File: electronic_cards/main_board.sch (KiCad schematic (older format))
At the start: 9 parts, among them J1 Input1, J2 Input2, J3 Esp8266, J4 Vin, J5 IN 5V, J6 Output1, J7 Output2

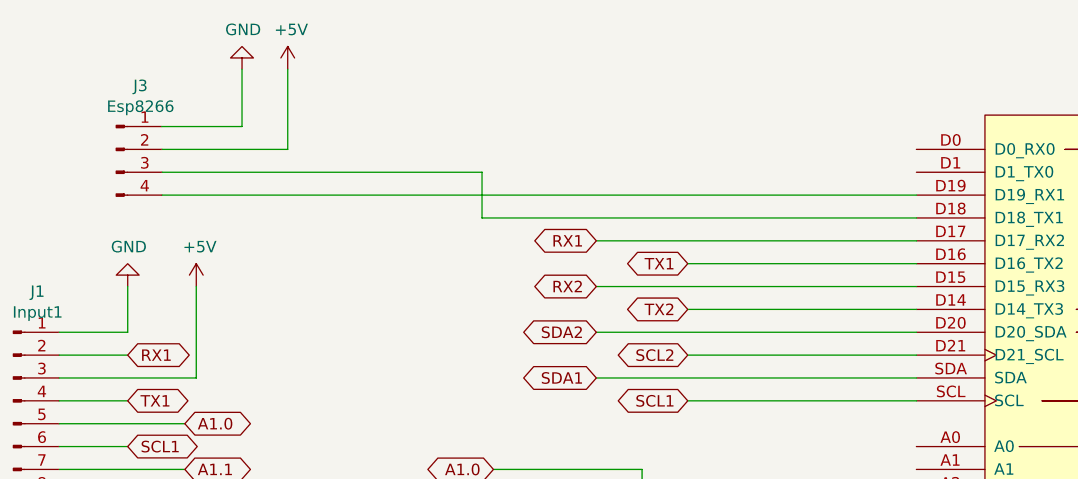
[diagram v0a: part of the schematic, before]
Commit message: Correctrion of PCB, RX and TX of ESP were inverted
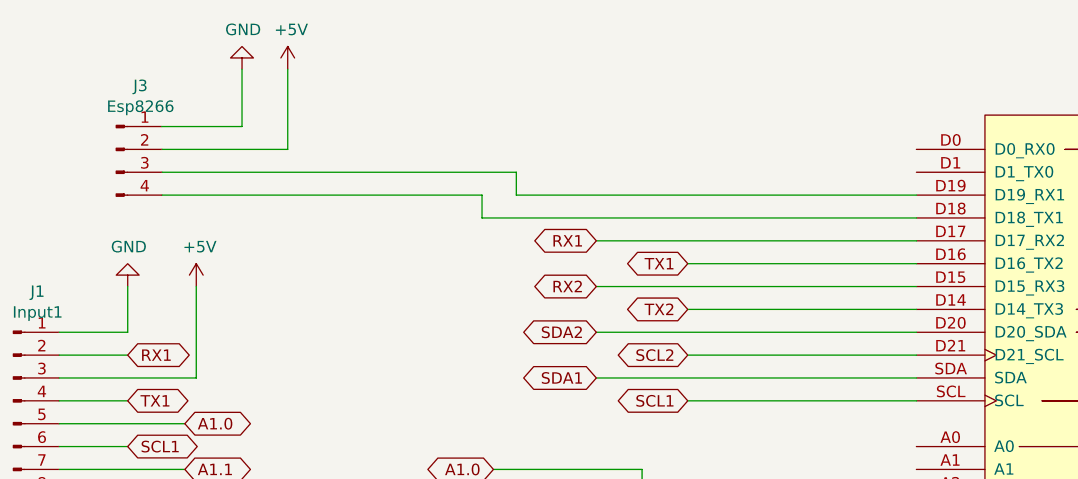
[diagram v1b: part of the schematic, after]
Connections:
- net at XA1.D18 (D18_TX1): now also J3.4 (Pin_4); no longer J3.3 (Pin_3)
- net at XA1.D19 (D19_RX1): now also J3.3 (Pin_3); no longer J3.4 (Pin_4)
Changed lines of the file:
@@
 Text GLabel 8300 3300 2    50   BiDi ~ 0
 I2.4
-Wire Wire Line
-	3500 1600 3500 1400
-Wire Wire Line
-	3500 1400 2100 1400
 Text GLabel 4000 1700 0    50   BiDi ~ 0
 RX1
@@
 Text GLabel 4400 2400 0    50   BiDi ~ 0
 SCL1
-Wire Wire Line
-	2100 1500 5400 1500
 Wire Wire Line
 	3500 1600 5400 1600
@@
 Wire Wire Line
 	8000 5600 8600 5600
+Wire Wire Line
+	2100 1500 3500 1500
+Wire Wire Line
+	3500 1500 3500 1600
+Wire Wire Line
+	2100 1400 3650 1400
+Wire Wire Line
+	3650 1400 3650 1500
+Wire Wire Line
+	3650 1500 5400 1500
 $EndSCHEMATC
